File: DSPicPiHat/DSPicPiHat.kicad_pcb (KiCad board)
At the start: 2 copper layers, 67 x 66.5 mm, 90 parts, among them J10 Nice!View, J4 Conn_PIC_ICSP_ICD, J5 USB_C_Receptacle_USB2.0, J6 PowerInput, J7 GenericSPIconn, J8 RasPiHeaders, J9 GeneralSPIDisplay, SW1 POWER_Select, SW2 SW_DIP_x08, U1 DSPIC33CH512MP508T-I_PT, U10 DF5A6.2CJE_LM, U11 FT230XS, U12 NCP1117-3.3_SOT223, U2 ISO1640BDR, U3 DF5A6.2CJE_LM, U4 DF5A6.2CJE_LM, U5 ISO1640BDR, U6 DF5A6.2CJE_LM, U7 DF5A6.2CJE_LM, U8 ISO1640BDR, U9 DF5A6.2CJE_LM

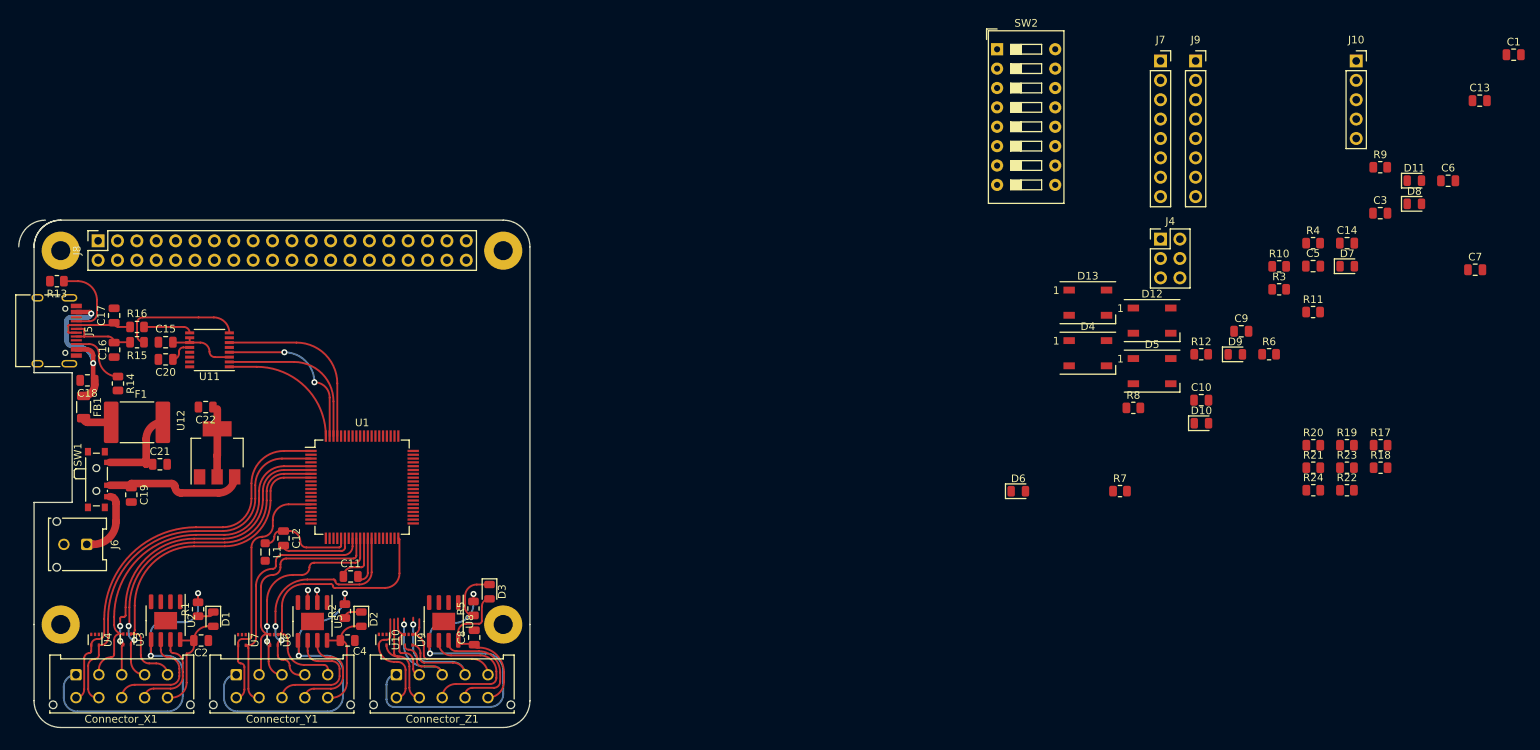
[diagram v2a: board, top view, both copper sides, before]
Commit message: PCB mostly routed
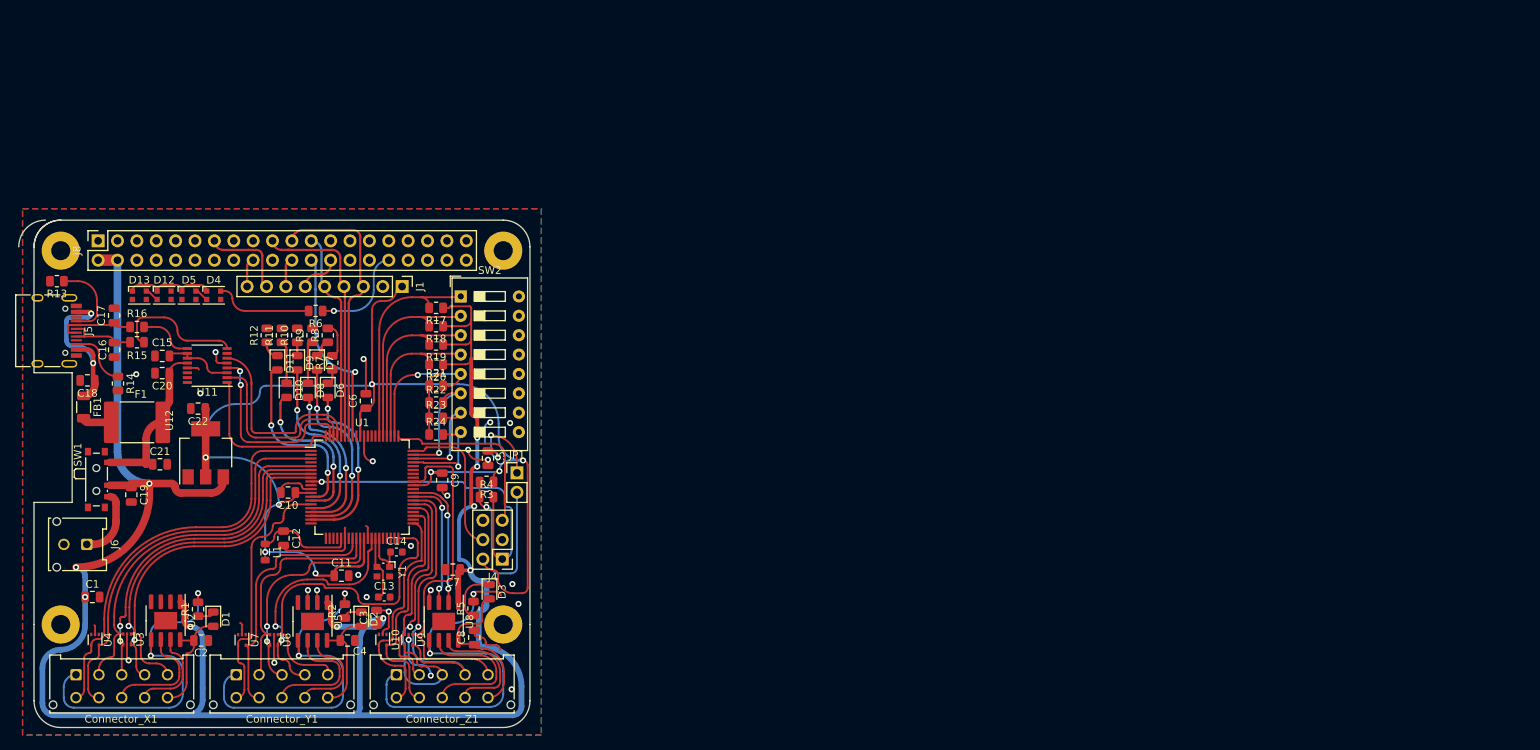
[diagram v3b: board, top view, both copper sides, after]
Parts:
- removed J10: Nice!View, Connector_PinSocket_2.54mm:PinSocket_1x05_P2.54mm_Vertical
- removed J7: GenericSPIconn, Connector_PinSocket_2.54mm:PinSocket_1x08_P2.54mm_Vertical
- removed J9: GeneralSPIDisplay, Connector_PinSocket_2.54mm:PinSocket_1x08_P2.54mm_Vertical
- added J1: Conn_01x09_Female, Connector_PinHeader_2.54mm:PinHeader_1x09_P2.54mm_Vertical, F.Cu at (104.8, 82.2)
- added JP1: Jumper_2_Open, Connector_PinHeader_2.54mm:PinHeader_1x02_P2.54mm_Vertical, F.Cu at (119.8, 106.6)
- added Y1: 16MHz, Crystal:Crystal_SMD_Abracon_ABM10-4Pin_2.5x2.0mm, F.Cu at (102.3, 119.6)
- C13, C14: footprint Capacitor_SMD:C_0805_2012Metric -> Capacitor_SMD:C_0603_1608Metric
- D12, D13, D4, D5: footprint LED_SMD:LED_WS2812B_PLCC4_5.0x5.0mm_P3.2mm -> LED_SMD:LED_WS2812B-2020_PLCC4_2.0x2.0mm
- L1: footprint Inductor_SMD:L_0805_2012Metric_Pad1.05x1.20mm_HandSolder -> Inductor_SMD:L_0805_2012Metric
- moved C1 199.4 mm to (64.2, 122.9)
- moved C13 157.6 mm to (102.4, 122.9)
- moved D11 150.9 mm to (88.4, 92.2), turned to -90 degrees
- moved D8 147.1 mm to (92.4, 95.8), turned to -90 degrees
- moved C6 144.8 mm to (100.0, 97.2), turned to 90 degrees
- moved C3 141.8 mm to (101.4, 125.6), turned to 90 degrees
- moved R9 141.7 mm to (93.0, 88.6), turned to 90 degrees
- moved C7 139.6 mm to (111.4, 119.3), turned to 180 degrees
- moved D7 135.6 mm to (93.6, 92.2), turned to -90 degrees
- moved R11 135.2 mm to (89.0, 88.6), turned to 90 degrees
- moved C14 131.0 mm to (104.0, 117.0)
- moved D12 129.5 mm to (73.5, 83.3)
- moved R10 129.0 mm to (91.0, 88.6), turned to 90 degrees
- moved D5 126.6 mm to (76.8, 83.3)
- moved R18 125.2 mm to (109.2, 87.4), turned to 180 degrees
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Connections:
- C1 pad 2: GNDZ -> AVSS
- C10 pad 2: VSS -> AVSS
- C11 pad 2: VSS -> AVSS
- C13 pad 2: GNDZ -> AVSS
- C14 pad 2: GNDZ -> AVSS
- C15 pad 2: GNDZ -> AVSS
- C16 pad 2: GNDZ -> AVSS
- C17 pad 2: GNDZ -> AVSS
- C18 pad 2: GNDZ -> AVSS
- C19 pad 2: GNDZ -> AVSS
- C2 pad 2: GND1 -> AVSS
- C20 pad 2: GNDZ -> AVSS
- C21 pad 2: GNDZ -> AVSS
- C22 pad 1: +3V3 -> VDD
- C22 pad 2: GNDZ -> AVSS
- C3 pad 2: GNDZ -> AVSS
- C4 pad 2: GND1 -> AVSS
- C5 pad 2: GNDZ -> AVSS
- C6 pad 2: VSS -> AVSS
- C7 pad 2: GNDZ -> AVSS
- C8 pad 2: GND1 -> AVSS
- C9 pad 2: VSS -> AVSS
- Connector_X1 pad 1: GNDZ -> AVSS
- Connector_Y1 pad 1: GNDZ -> AVSS
- Connector_Z1 pad 1: GNDZ -> AVSS
- D12 pad 3: GNDZ -> AVSS
- D13 pad 3: GNDZ -> AVSS
- D4 pad 3: GNDZ -> AVSS
- D5 pad 3: GNDZ -> AVSS
- J4 pad 2: +3V3 -> VDD
- J4 pad 3: GNDZ -> AVSS
- J5 pad A1: GNDZ -> AVSS
- J5 pad A12: GNDZ -> AVSS
- J5 pad B1: GNDZ -> AVSS
- J5 pad B12: GNDZ -> AVSS
- J5 pad S1: GNDZ -> AVSS
- J6 pad 2: GNDZ -> AVSS
- J8 pad 14: GNDZ -> AVSS
- J8 pad 20: GNDZ -> AVSS
- J8 pad 25: GNDZ -> AVSS
- J8 pad 30: GNDZ -> AVSS
- J8 pad 34: GNDZ -> AVSS
- J8 pad 39: GNDZ -> AVSS
- J8 pad 6: GNDZ -> AVSS
- J8 pad 9: GNDZ -> AVSS
- R1 pad 2: GNDZ -> AVSS
- R10 pad 2: GNDZ -> AVSS
- R11 pad 2: GNDZ -> AVSS
- R12 pad 2: GNDZ -> AVSS
- R13 pad 2: GNDZ -> AVSS
- R14 pad 2: GNDZ -> AVSS
- R2 pad 2: GNDZ -> AVSS
- R3 pad 1: +3V3 -> VDD
- R5 pad 2: GNDZ -> AVSS
- R7 pad 2: GNDZ -> AVSS
- R8 pad 2: GNDZ -> AVSS
- R9 pad 2: GNDZ -> AVSS
- SW2 pad 10: GNDZ -> AVSS
- SW2 pad 11: GNDZ -> AVSS
- SW2 pad 12: GNDZ -> AVSS
- SW2 pad 13: GNDZ -> AVSS
- SW2 pad 14: GNDZ -> AVSS
- SW2 pad 15: GNDZ -> AVSS
- SW2 pad 16: GNDZ -> AVSS
- SW2 pad 9: GNDZ -> AVSS
- U1 pad 11: VSS -> AVSS
- U1 pad 13: unconnected-(U1-Pad13) -> dsPIC_LED_05
- U1 pad 14: unconnected-(U1-Pad14) -> dsPIC_LED_04
- U1 pad 16: DIP_00 -> dsPIC_LED_03
- U1 pad 17: DIP_01 -> dsPIC_LED_02
- U1 pad 18: DIP_02 -> dsPIC_LED_01
- U1 pad 19: DIP_03 -> dsPIC_LED_00
- U1 pad 20: DIP_04 -> unconnected-(U1-Pad20)
- U1 pad 21: DIP_05 -> unconnected-(U1-Pad21)
- U1 pad 22: DIP_06 -> unconnected-(U1-Pad22)
- U1 pad 23: DIP_07 -> unconnected-(U1-Pad23)
- U1 pad 32: VSS -> AVSS
- U1 pad 36: dsPIC_LED_00 -> unconnected-(U1-Pad36)
- U1 pad 37: dsPIC_LED_01 -> unconnected-(U1-Pad37)
- U1 pad 38: dsPIC_LED_02 -> unconnected-(U1-Pad38)
- U1 pad 39: dsPIC_LED_03 -> unconnected-(U1-Pad39)
- U1 pad 41: unconnected-(U1-Pad41) -> EXT_Z_PWM_00
- U1 pad 42: dsPIC_LED_04 -> unconnected-(U1-Pad42)
- U1 pad 43: unconnected-(U1-Pad43) -> EXT_Z_PWM_01
- U1 pad 44: dsPIC_LED_05 -> unconnected-(U1-Pad44)
- U1 pad 45: unconnected-(U1-Pad45) -> EXT_ADC_Z_00
- U1 pad 46: unconnected-(U1-Pad46) -> EXT_ADC_Z_01
- U1 pad 47: unconnected-(U1-Pad47) -> EXT_ADC_Z_02
- U1 pad 50: VSS -> AVSS
- U1 pad 52: unconnected-(U1-Pad52) -> EXT_ADC_Z_03
- U1 pad 55: PI_CE0 -> unconnected-(U1-Pad55)
- U1 pad 56: PI_MOSI -> unconnected-(U1-Pad56)
- U1 pad 57: unconnected-(U1-Pad57) -> DIP_07
- U1 pad 58: unconnected-(U1-Pad58) -> DIP_06
- U1 pad 59: unconnected-(U1-Pad59) -> DIP_05
- U1 pad 62: unconnected-(U1-Pad62) -> DIP_04
- U1 pad 63: EXT_ADC_Z_00 -> DIP_03
- U1 pad 64: EXT_Z_PWM_01 -> DIP_02
- U1 pad 65: EXT_ADC_Z_01 -> DIP_01
- U1 pad 66: EXT_ADC_Z_02 -> unconnected-(U1-Pad66)
- U1 pad 67: EXT_ADC_Z_03 -> unconnected-(U1-Pad67)
- U1 pad 70: VSS -> AVSS
- U1 pad 73: unconnected-(U1-Pad73) -> PI_CE0
- U1 pad 74: EXT_Z_PWM_00 -> PI_MISO
- U1 pad 75: PI_MISO -> PI_MOSI
- U10 pad 2: GNDZ -> AVSS
- U11 pad 13: GNDZ -> AVSS
- U11 pad 5: GNDZ -> AVSS
- U12 pad 1: GNDZ -> AVSS
- U12 pad 2: +3V3 -> VDD
- U2 pad 4: GNDZ -> AVSS
- U2 pad 5: GNDZ -> AVSS
- U3 pad 2: GNDZ -> AVSS
- U4 pad 2: GNDZ -> AVSS
- U5 pad 4: GNDZ -> AVSS
- U5 pad 5: GNDZ -> AVSS
- U6 pad 2: GNDZ -> AVSS
- U7 pad 2: GNDZ -> AVSS
- U8 pad 4: GNDZ -> AVSS
- U8 pad 5: GNDZ -> AVSS
- U9 pad 2: GNDZ -> AVSS
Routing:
- net +5V: track 18.3 -> 302.2 mm, vias 0 -> 10
- net AVSS: track 9.87 -> 216.8 mm, vias 0 -> 28
- net VDD: track 6.97 -> 177.2 mm, vias 0 -> 8
- net GNDZ: track 141.3 -> 0.00 mm, vias 6 -> 0
- net MCLR: track 0.00 -> 44.6 mm, vias 0 -> 1
- net PI_MISO: track 0.00 -> 36.7 mm
- net PI_MOSI: track 0.00 -> 33.9 mm
- net EXT_ADC_Z_03: track 15.8 -> 45.6 mm
- net DIP_00: track 0.00 -> 28.9 mm
- net PI_SCLK: track 0.00 -> 27.7 mm
- net DIP_01: track 0.00 -> 26.3 mm
- net PI_CE0: track 0.00 -> 26.2 mm, vias 0 -> 1
- net Net-(JP1-Pad2): track 0.00 -> 26.0 mm, vias 0 -> 1
- net dsPIC_LED_01: track 0.00 -> 25.9 mm, vias 0 -> 2
- net dsPIC_LED_05: track 0.00 -> 24.3 mm, vias 0 -> 2
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- added copper zone on B.Cu, net AVSS
- added copper zone on F.Cu, net AVSS

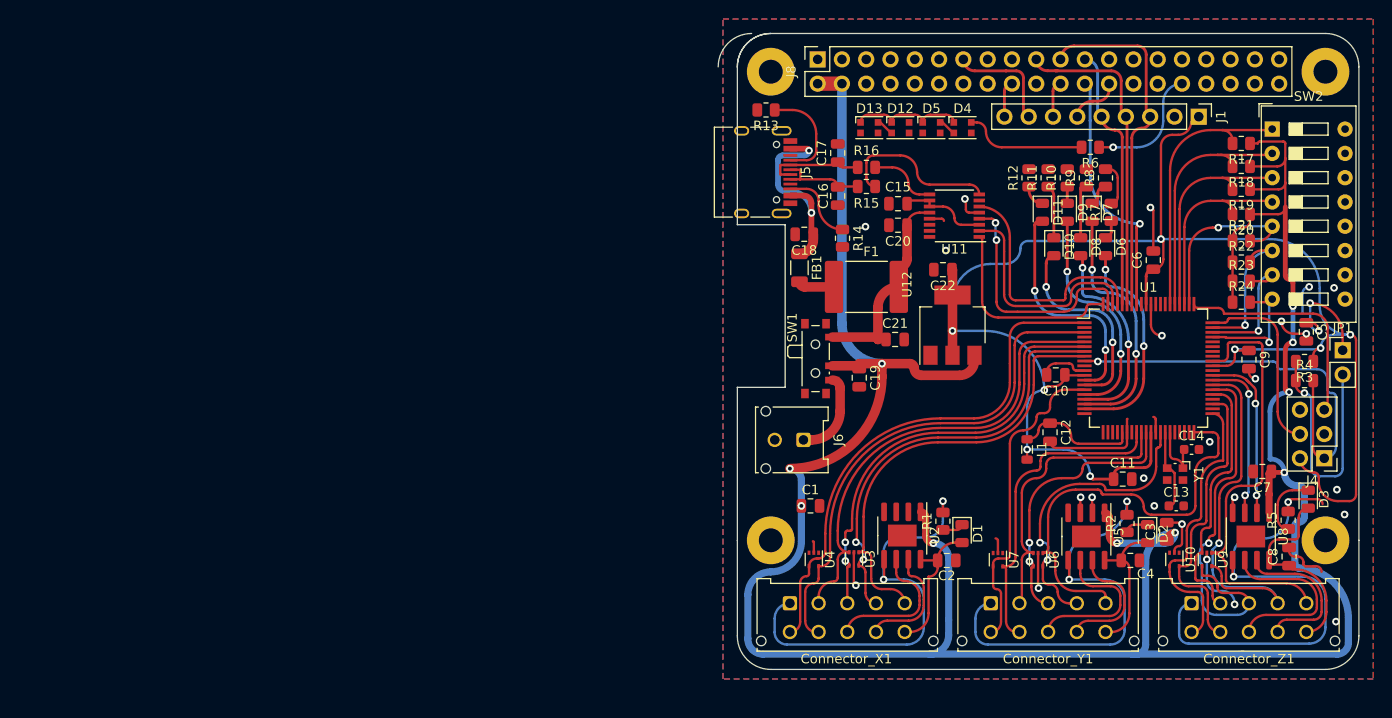
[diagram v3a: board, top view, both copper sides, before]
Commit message: changed connectors and removed i2c lines and i2c isolator.
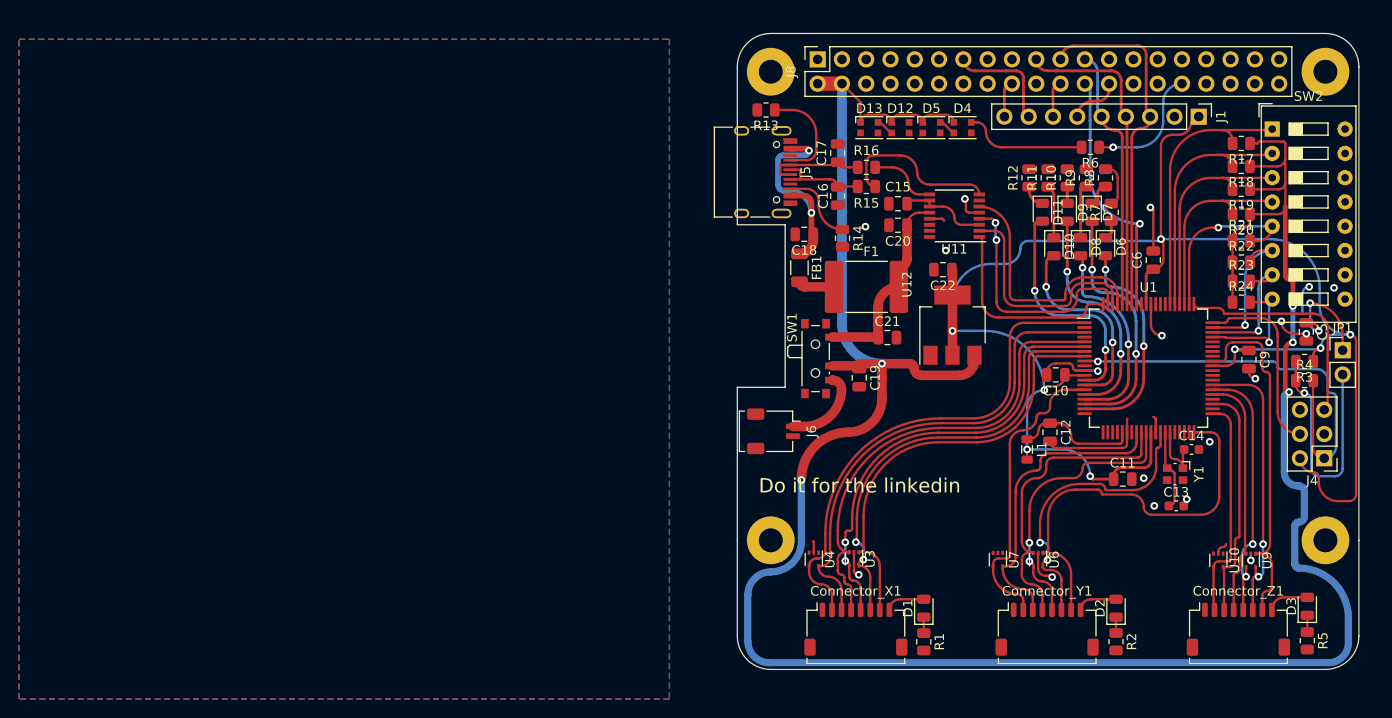
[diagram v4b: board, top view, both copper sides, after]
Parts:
- removed C1, C2, C3, C4, C7, C8: 0.1uf, Capacitor_SMD:C_0805_2012Metric
- removed U2, U5, U8: ISO1640BDR, Package_SO:SOIC-8-1EP_3.9x4.9mm_P1.27mm_EP2.29x3mm
- added G***: LOGO, cubepattern:husky, B.Cu at (102.0, 97.2)
- Connector_X1, Connector_Y1, Connector_Z1: value Conn_01x10 -> Conn_01x08; footprint Connector_Molex:Molex_Micro-Fit_3.0_43045-1012_2x05_P3.00mm_Vertical -> Connector_Molex:Molex_Pico-Clasp_202396-0807_1x08-1MP_P1.00mm_Horizontal
- J6: footprint Connector_Molex:Molex_Micro-Fit_3.0_43045-0212_2x01_P3.00mm_Vertical -> Connector_Molex:Molex_Pico-Clasp_202396-0207_1x02-1MP_P1.00mm_Horizontal
- moved R1 12.8 mm to (76.0, 137.1), turned to -90 degrees
- moved R5 12.8 mm to (116.1, 137.0), turned to -90 degrees
- moved R2 12.4 mm to (96.1, 137.1), turned to -90 degrees
- moved D3 11.2 mm to (116.1, 133.4), turned to 90 degrees
- moved D1 8.77 mm to (76.0, 133.6), turned to 90 degrees
- moved D2 8.47 mm to (96.1, 133.6), turned to 90 degrees
- moved Connector_X1 7.41 mm to (68.9, 135.8)
- moved Connector_Y1 6.49 mm to (88.9, 135.8)
- moved Connector_Z1 5.60 mm to (108.9, 135.8)
- moved U9 4.60 mm to (110.2, 128.6)
- moved U10 4.60 mm to (106.8, 128.6)
- moved J6 3.24 mm to (60.3, 115.1)
- moved C21 0.82 mm to (72.2, 105.3)
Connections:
- Connector_X1 pad 2: EXT_ADC_X_00 -> EXT_X_PWM_00
- Connector_X1 pad 3: EXT_ADC_X_01 -> EXT_X_PWM_01
- Connector_X1 pad 4: EXT_ADC_X_02 -> EXT_ADC_X_00
- Connector_X1 pad 5: EXT_ADC_X_03 -> EXT_ADC_X_01
- Connector_X1 pad 6: EXT_X_PWM_00 -> EXT_ADC_X_02
- Connector_X1 pad 7: EXT_X_PWM_01 -> EXT_ADC_X_03
- Connector_X1 pad 8: EXT_X_SCL -> 5vX
- Connector_Y1 pad 2: EXT_ADC_Y_00 -> EXT_Y_PWM_00
- Connector_Y1 pad 3: EXT_ADC_Y_01 -> EXT_Y_PWM_01
- Connector_Y1 pad 4: EXT_ADC_Y_02 -> EXT_ADC_Y_00
- Connector_Y1 pad 5: EXT_ADC_Y_03 -> EXT_ADC_Y_01
- Connector_Y1 pad 6: EXT_Y_PWM_00 -> EXT_ADC_Y_02
- Connector_Y1 pad 7: EXT_Y_PWM_01 -> EXT_ADC_Y_03
- Connector_Y1 pad 8: EXT_Y_SCL -> 5vY
- Connector_Z1 pad 2: EXT_ADC_Z_00 -> EXT_Z_PWM_00
- Connector_Z1 pad 3: EXT_ADC_Z_01 -> EXT_Z_PWM_01
- Connector_Z1 pad 4: EXT_ADC_Z_02 -> EXT_ADC_Z_00
- Connector_Z1 pad 5: EXT_ADC_Z_03 -> EXT_ADC_Z_01
- Connector_Z1 pad 6: EXT_Z_PWM_00 -> EXT_ADC_Z_02
- Connector_Z1 pad 7: EXT_Z_PWM_01 -> EXT_ADC_Z_03
- Connector_Z1 pad 8: EXT_Z_SCL -> 5vZ
- U1 pad 48: INT_SCL -> unconnected-(U1-Pad48)
- U1 pad 49: INT_SDA -> unconnected-(U1-Pad49)
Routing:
- net AVSS: track 216.8 -> 54.8 mm, vias 28 -> 18
- net +5V: track 302.2 -> 254.2 mm, vias 10 -> 5
- net INT_SDA: track 20.1 -> 0.00 mm, vias 3 -> 0
- net EXT_Z_SCL: track 19.2 -> 0.00 mm
- net INT_SCL: track 18.9 -> 0.00 mm, vias 3 -> 0
- net EXT_Y_SCL: track 16.8 -> 0.00 mm
- net 5vZ: track 21.0 -> 4.40 mm
- net EXT_Z_SDA: track 16.2 -> 0.00 mm
- net EXT_X_SCL: track 15.1 -> 0.00 mm
- net EXT_Y_SDA: track 13.2 -> 0.00 mm
- net EXT_X_SDA: track 12.2 -> 0.00 mm
- net EXT_ADC_Z_01: track 40.0 -> 27.9 mm, vias 1 -> 2
- net EXT_ADC_Z_02: track 41.2 -> 30.0 mm, vias 1 -> 2
- net 5vX: track 15.0 -> 4.19 mm
- net 5vY: track 15.0 -> 4.29 mm
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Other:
- board size 67 x 66.5 mm -> 65 x 66.5 mm
- board text added: "Do it for the linkedin"
